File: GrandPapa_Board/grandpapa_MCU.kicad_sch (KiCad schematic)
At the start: 23 parts, among them J6 Conn_02x06, U10 MCP2515, U7 MCP2562, U8 MCP2562, U9 PIC18F26K83, Y1 12MHz

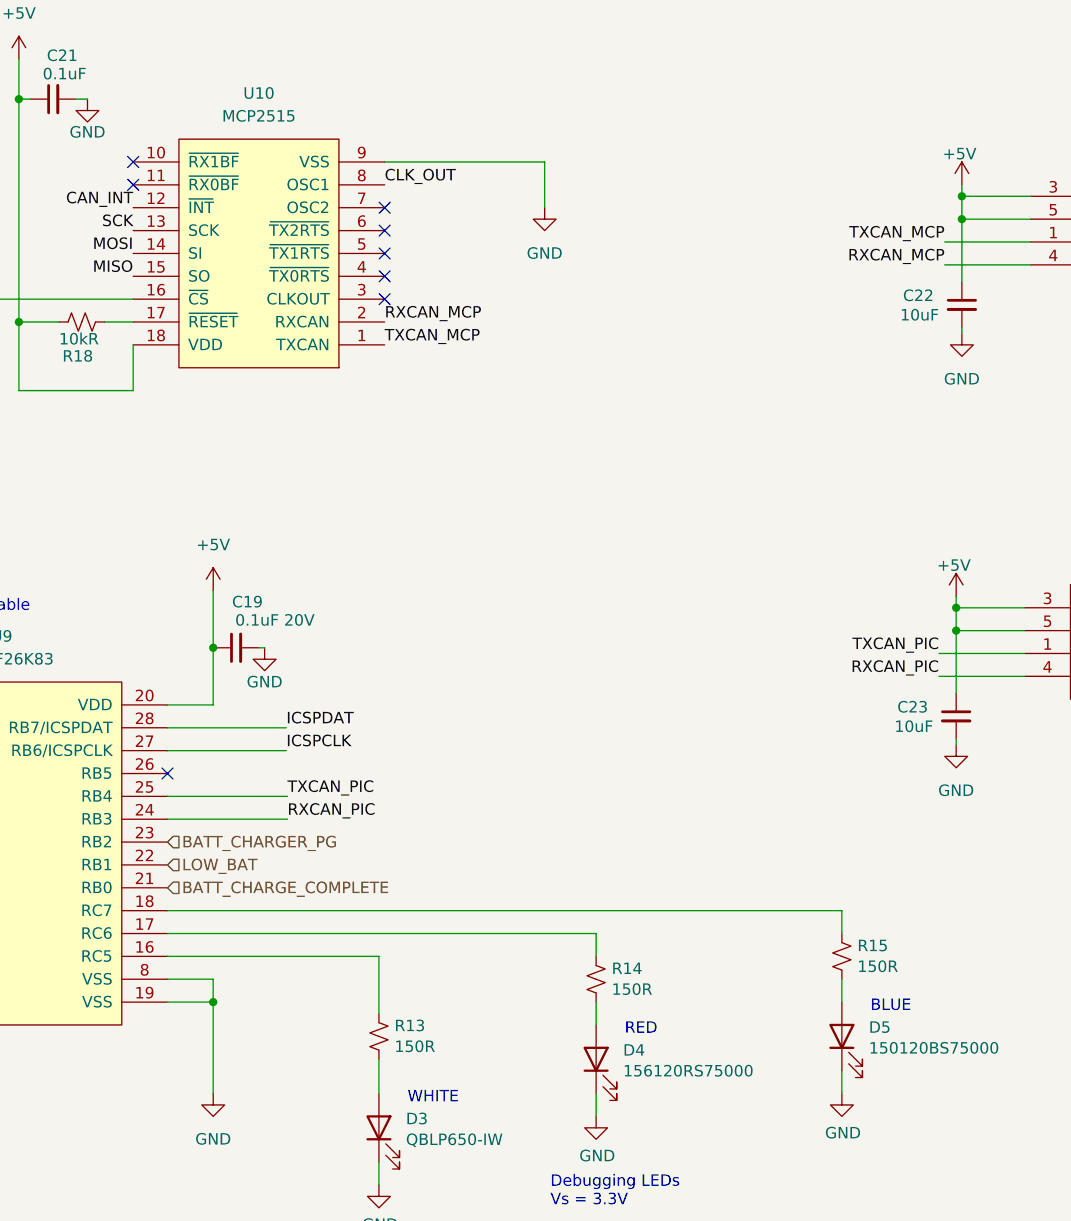
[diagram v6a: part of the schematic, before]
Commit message: minor fixes; chip shortage tearing me a new one
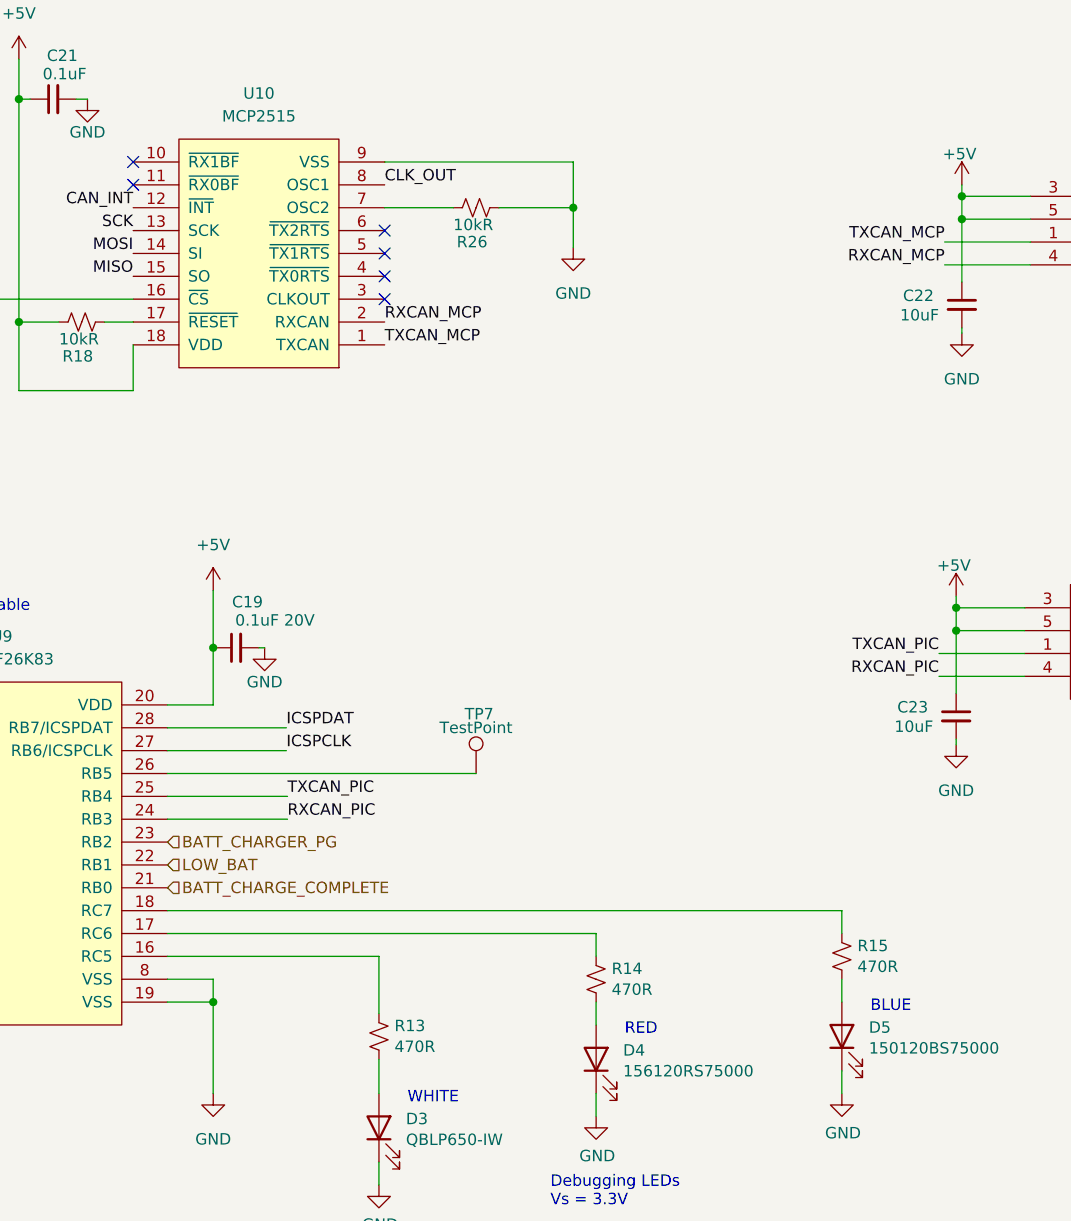
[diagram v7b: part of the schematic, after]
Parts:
- added R26: 10kR, symbol Device:R_Small_US
- added TP7: TestPoint, symbol Connector:TestPoint
- R13, R14, R15: value 150R -> 470R
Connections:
- net GND: now also R26.2
- net at U10.7 (OSC2): now also R26.1
- net at U9.26 (RB5): now also TP7.1
- no-connect marks 8 -> 6
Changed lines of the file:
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@@
   (junction (at 250.825 99.695) (diameter 0) (color 0 0 0 0)
+  )
+  (junction (at 172.085 47.625) (diameter 0) (color 0 0 0 0)
   )
   (junction (at 215.265 46.355) (diameter 0) (color 0 0 0 0)
@@
   (no_connect (at 123.19 42.545))
   (no_connect (at 123.19 45.085))
-  (no_connect (at 151.13 47.625))
   (no_connect (at 151.13 50.165))
   (no_connect (at 151.13 52.705))
   (no_connect (at 151.13 55.245))
   (no_connect (at 151.13 57.785))
-  (no_connect (at 127 110.49))
   (wire (pts (xy 250.825 99.695) (xy 250.825 92.075))
     (stroke (width 0) (type default) (color 0 0 0 0))
@@
     (stroke (width 0) (type default) (color 0 0 0 0))
   )
+  (wire (pts (xy 151.13 47.625) (xy 158.75 47.625))
+    (stroke (width 0) (type default) (color 0 0 0 0))
+  )
   (wire (pts (xy 127 133.35) (xy 132.08 133.35))
     (stroke (width 0) (type default) (color 0 0 0 0))
@@
     (stroke (width 0) (type default) (color 0 0 0 0))
   )
-  (wire (pts (xy 168.91 42.545) (xy 168.91 47.625))
+  (wire (pts (xy 172.085 42.545) (xy 172.085 47.625))
     (stroke (width 0) (type default) (color 0 0 0 0))
   )
@@
     (stroke (width 0) (type default) (color 0 0 0 0))
   )
+  (wire (pts (xy 172.085 47.625) (xy 172.085 52.07))
+    (stroke (width 0) (type default) (color 0 0 0 0))
+  )
   (wire (pts (xy 87.63 113.03) (xy 90.17 113.03))
     (stroke (width 0) (type default) (color 0 0 0 0))
@@
     (stroke (width 0) (type default) (color 0 0 0 0))
   )
+  (wire (pts (xy 163.83 47.625) (xy 172.085 47.625))
+    (stroke (width 0) (type default) (color 0 0 0 0))
+  )
   (wire (pts (xy 29.21 45.72) (xy 44.45 45.72))
     (stroke (width 0) (type default) (color 0 0 0 0))
@@
     (stroke (width 0) (type default) (color 0 0 0 0))
   )
+  (wire (pts (xy 127 110.49) (xy 161.29 110.49))
+    (stroke (width 0) (type default) (color 0 0 0 0))
+  )
   (wire (pts (xy 137.16 96.52) (xy 137.795 96.52))
     (stroke (width 0) (type default) (color 0 0 0 0))
@@
     (stroke (width 0) (type default) (color 0 0 0 0))
   )
-  (wire (pts (xy 151.13 42.545) (xy 168.91 42.545))
+  (wire (pts (xy 151.13 42.545) (xy 172.085 42.545))
     (stroke (width 0) (type default) (color 0 0 0 0))
   )
@@
     (pin "1")
   )
+  (symbol (lib_id "Device:R_Small_US") (at 161.29 47.625 90) (unit 1)
+    (in_bom yes) (on_board yes)
+    (property "Reference" "R26" (id 0) (at 162.56 51.435 90)
+      (effects (font (size 1.27 1.27)) (justify left))
+    )
+    (property "Value" "10kR" (id 1) (at 163.195 49.53 90)
+      (effects (font (size 1.27 1.27)) (justify left))
+    )
+    (property "Footprint" "" (id 2) (at 161.29 47.625 0)
+      (effects (font (size 1.27 1.27)) hide)
+    )
+    (property "Datasheet" "~" (id 3) (at 161.29 47.625 0)
+      (effects (font (size 1.27 1.27)) hide)
+    )
+    (pin "1")
+    (pin "2")
+  )
   (symbol (lib_id "Device:R_Small_US") (at 174.625 133.35 0) (unit 1)
     (in_bom yes) (on_board yes)
@@
       (effects (font (size 1.27 1.27)) (justify left))
     )
-    (property "Value" "150R" (id 1) (at 176.3522 134.493 0)
+    (property "Value" "470R" (id 1) (at 176.3522 134.493 0)
       (effects (font (size 1.27 1.27)) (justify left))
     )
@@
     (pin "2")
   )
-  (symbol (lib_id "power:GND") (at 168.91 47.625 0) (unit 1)
-    (in_bom yes) (on_board yes) (fields_autoplaced)
-    (property "Reference" "#PWR0108" (id 0) (at 168.91 53.975 0)
-      (effects (font (size 1.27 1.27)) hide)
-    )
-    (property "Value" "GND" (id 1) (at 168.91 52.705 0))
-    (property "Footprint" "" (id 2) (at 168.91 47.625 0)
-      (effects (font (size 1.27 1.27)) hide)
-    )
-    (property "Datasheet" "" (id 3) (at 168.91 47.625 0)
+  (symbol (lib_id "power:GND") (at 172.085 52.07 0) (unit 1)
+    (in_bom yes) (on_board yes) (fields_autoplaced)
+    (property "Reference" "#PWR0108" (id 0) (at 172.085 58.42 0)
+      (effects (font (size 1.27 1.27)) hide)
+    )
+    (property "Value" "GND" (id 1) (at 172.085 57.15 0))
+    (property "Footprint" "" (id 2) (at 172.085 52.07 0)
+      (effects (font (size 1.27 1.27)) hide)
+    )
+    (property "Datasheet" "" (id 3) (at 172.085 52.07 0)
       (effects (font (size 1.27 1.27)) hide)
     )
@@
       (effects (font (size 1.27 1.27)) (justify left))
     )
-    (property "Value" "150R" (id 1) (at 152.2222 140.843 0)
+    (property "Value" "470R" (id 1) (at 152.2222 140.843 0)
       (effects (font (size 1.27 1.27)) (justify left))
     )
@@
       (effects (font (size 1.27 1.27)) (justify left))
     )
-    (property "Value" "150R" (id 1) (at 203.6572 131.953 0)
+    (property "Value" "470R" (id 1) (at 203.6572 131.953 0)
       (effects (font (size 1.27 1.27)) (justify left))
     )
@@
     (pin "2")
   )
+  (symbol (lib_id "Connector:TestPoint") (at 161.29 110.49 0) (unit 1)
+    (in_bom yes) (on_board yes)
+    (property "Reference" "TP7" (id 0) (at 160.02 103.886 0)
+      (effects (font (size 1.27 1.27)) (justify left))
+    )
+    (property "Value" "TestPoint" (id 1) (at 157.226 105.41 0)
+      (effects (font (size 1.27 1.27)) (justify left))
+    )
+    (property "Footprint" "" (id 2) (at 166.37 110.49 0)
+      (effects (font (size 1.27 1.27)) hide)
+    )
+    (property "Datasheet" "~" (id 3) (at 166.37 110.49 0)
+      (effects (font (size 1.27 1.27)) hide)
+    )
+    (pin "1")
+  )
   (symbol (lib_id "power:+5V") (at 215.265 45.085 0) (unit 1)
